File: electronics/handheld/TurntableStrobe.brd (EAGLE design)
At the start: 25.1 x 17.8 mm, 18 parts, among them IC1 TINY25, J1 ISP, Q1 12MHz

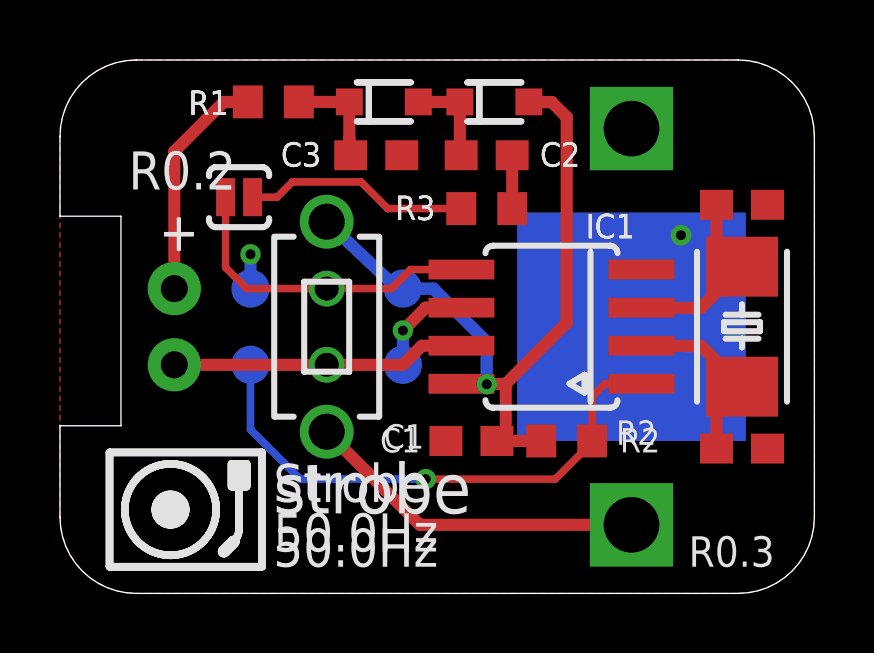
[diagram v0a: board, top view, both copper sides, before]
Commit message: diode array replaces discrete
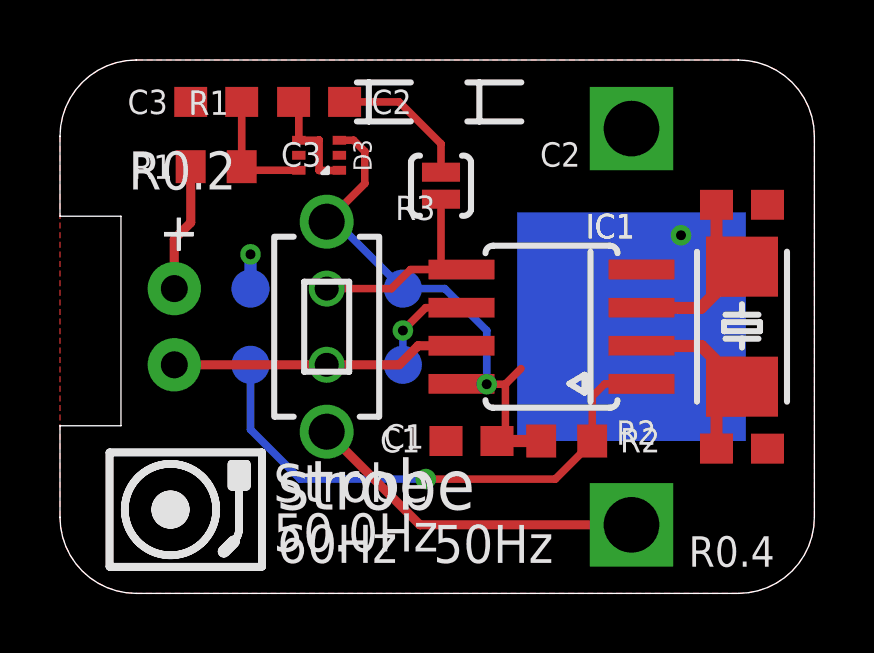
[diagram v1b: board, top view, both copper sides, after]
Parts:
- removed D1, D2: 1N4148, bt_diode:SOD-323
- removed R3: 100, rcl:R0603
- added D3: BAT54V, bt_diode:SOT-563
- moved JP1 6.74 mm to (12.7, 13.6), turned to 90 degrees
- moved C2 5.86 mm to (8.64, 16.4)
- moved C3 5.62 mm to (5.21, 16.4), turned to 180 degrees
- moved R1 2.88 mm to (5.21, 14.2)
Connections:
- removed net N$1: JP1.2, R3.2
- net N$2: now also D3.1, D3.4; no longer D1.C, D2.A
- net N$4: now also JP1.2; no longer R3.1
- net VCC: now also D3.3; no longer D1.A
- net VHI: now also D3.6; no longer D2.C
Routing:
- net N$1: track 7.53 -> 0.00 mm
- net VCC: track 24.6 -> 18.7 mm
- net PB0: track 10.8 -> 7.10 mm
- net N$3: track 7.71 -> 4.29 mm
- net N$4: track 1.78 -> 4.74 mm
- net VHI: track 3.46 -> 4.11 mm
- net N$2: track 3.16 -> 3.72 mm
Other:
- board text added: "50Hz"
- board text added: "60Hz"
- board text added: "R0.4"
- board text removed: "R0.3"
